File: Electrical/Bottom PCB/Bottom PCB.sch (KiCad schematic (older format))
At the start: 38 parts, among them J101 Steper1, J102 Steper2, SW101 FL, SW102 FR, U101 QRE1113, U102 ULN2003A, U103 MCP23017_SO, U104 QRE1113, U105 QRE1113, U106 QRE1113

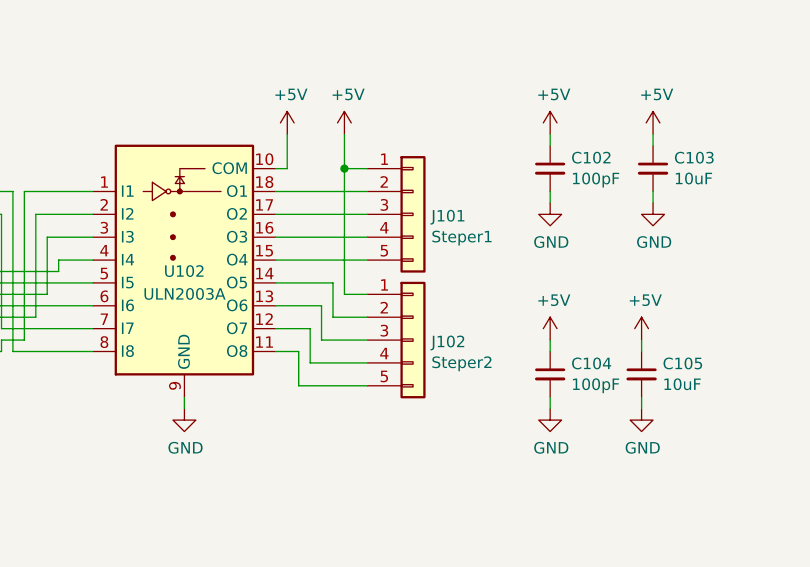
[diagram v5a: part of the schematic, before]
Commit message: changed from 1206 to 0805
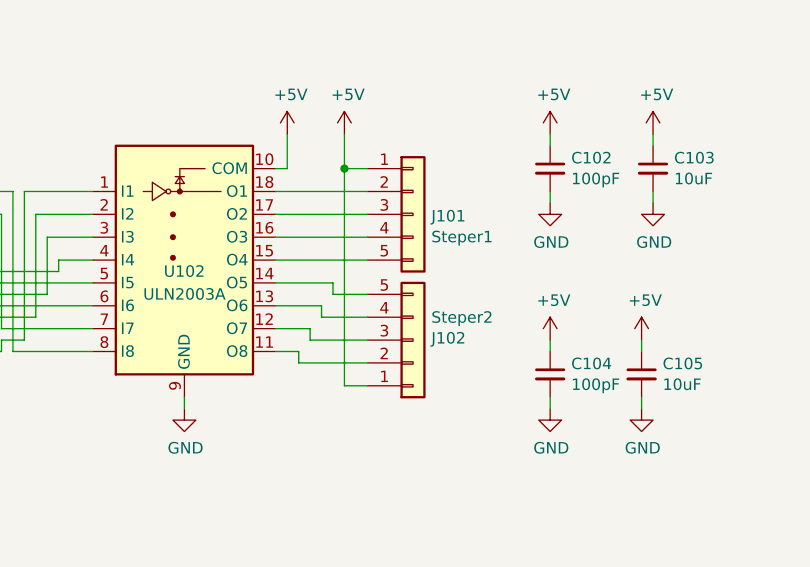
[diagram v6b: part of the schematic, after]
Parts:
- C101, C102, C103, C104, C105, C106, C107, C108: footprint Capacitor_SMD:C_1206_3216Metric_Pad1.42x1.75mm_HandSolder -> Capacitor_SMD:C_0805_2012Metric_Pad1.15x1.40mm_HandSolder
- R101, R102, R103, R104, R105, R106, R107, R108, R109, R110, R111, R112, R113, R114, R115: footprint Resistor_SMD:R_1206_3216Metric_Pad1.42x1.75mm_HandSolder -> Resistor_SMD:R_0805_2012Metric_Pad1.15x1.40mm_HandSolder
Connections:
- net at U102.11 (O8): now also J102.2 (Pin_2); no longer J102.5 (Pin_5)
- net at U102.12 (O7): now also J102.3 (Pin_3); no longer J102.4 (Pin_4)
- net at U102.13 (O6): now also J102.4 (Pin_4); no longer J102.3 (Pin_3)
- net at U102.14 (O5): now also J102.5 (Pin_5); no longer J102.2 (Pin_2)
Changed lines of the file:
@@
 F 0 "R104" H 1041 1904 50  0000 R CNN
 F 1 "10k" H 1041 1995 50  0000 R CNN
-F 2 "Resistor_SMD:R_1206_3216Metric_Pad1.42x1.75mm_HandSolder" H 1100 1950 50  0001 C CNN
+F 2 "Resistor_SMD:R_0805_2012Metric_Pad1.15x1.40mm_HandSolder" H 1100 1950 50  0001 C CNN
 F 3 "~" H 1100 1950 50  0001 C CNN
 	1    1100 1950
@@
 F 0 "R101" H 1041 1004 50  0000 R CNN
 F 1 "10k" H 1041 1095 50  0000 R CNN
-F 2 "Resistor_SMD:R_1206_3216Metric_Pad1.42x1.75mm_HandSolder" H 1100 1050 50  0001 C CNN
+F 2 "Resistor_SMD:R_0805_2012Metric_Pad1.15x1.40mm_HandSolder" H 1100 1050 50  0001 C CNN
 F 3 "~" H 1100 1050 50  0001 C CNN
 	1    1100 1050
@@
 F 0 "R106" H 1341 2704 50  0000 R CNN
 F 1 "10k" H 1341 2795 50  0000 R CNN
-F 2 "Resistor_SMD:R_1206_3216Metric_Pad1.42x1.75mm_HandSolder" H 1400 2750 50  0001 C CNN
+F 2 "Resistor_SMD:R_0805_2012Metric_Pad1.15x1.40mm_HandSolder" H 1400 2750 50  0001 C CNN
 F 3 "~" H 1400 2750 50  0001 C CNN
 	1    1400 2750
@@
 F 0 "R105" H 608 2704 50  0000 L CNN
 F 1 "100" H 608 2795 50  0000 L CNN
-F 2 "Resistor_SMD:R_1206_3216Metric_Pad1.42x1.75mm_HandSolder" H 550 2750 50  0001 C CNN
+F 2 "Resistor_SMD:R_0805_2012Metric_Pad1.15x1.40mm_HandSolder" H 550 2750 50  0001 C CNN
 F 3 "~" H 550 2750 50  0001 C CNN
 	1    550  2750
@@
 F 0 "C101" H 1492 3146 50  0000 L CNN
 F 1 "100pF" H 1492 3055 50  0000 L CNN
-F 2 "Capacitor_SMD:C_1206_3216Metric_Pad1.42x1.75mm_HandSolder" H 1400 3100 50  0001 C CNN
+F 2 "Capacitor_SMD:C_0805_2012Metric_Pad1.15x1.40mm_HandSolder" H 1400 3100 50  0001 C CNN
 F 3 "~" H 1400 3100 50  0001 C CNN
 	1    1400 3100
@@
 F 0 "R108" H 1341 4004 50  0000 R CNN
 F 1 "10k" H 1341 4095 50  0000 R CNN
-F 2 "Resistor_SMD:R_1206_3216Metric_Pad1.42x1.75mm_HandSolder" H 1400 4050 50  0001 C CNN
+F 2 "Resistor_SMD:R_0805_2012Metric_Pad1.15x1.40mm_HandSolder" H 1400 4050 50  0001 C CNN
 F 3 "~" H 1400 4050 50  0001 C CNN
 	1    1400 4050
@@
 F 0 "R107" H 608 4004 50  0000 L CNN
 F 1 "100" H 608 4095 50  0000 L CNN
-F 2 "Resistor_SMD:R_1206_3216Metric_Pad1.42x1.75mm_HandSolder" H 550 4050 50  0001 C CNN
+F 2 "Resistor_SMD:R_0805_2012Metric_Pad1.15x1.40mm_HandSolder" H 550 4050 50  0001 C CNN
 F 3 "~" H 550 4050 50  0001 C CNN
 	1    550  4050
@@
 F 0 "C106" H 1492 4446 50  0000 L CNN
 F 1 "100pF" H 1492 4355 50  0000 L CNN
-F 2 "Capacitor_SMD:C_1206_3216Metric_Pad1.42x1.75mm_HandSolder" H 1400 4400 50  0001 C CNN
+F 2 "Capacitor_SMD:C_0805_2012Metric_Pad1.15x1.40mm_HandSolder" H 1400 4400 50  0001 C CNN
 F 3 "~" H 1400 4400 50  0001 C CNN
 	1    1400 4400
@@
 F 0 "R113" H 1341 5254 50  0000 R CNN
 F 1 "10k" H 1341 5345 50  0000 R CNN
-F 2 "Resistor_SMD:R_1206_3216Metric_Pad1.42x1.75mm_HandSolder" H 1400 5300 50  0001 C CNN
+F 2 "Resistor_SMD:R_0805_2012Metric_Pad1.15x1.40mm_HandSolder" H 1400 5300 50  0001 C CNN
 F 3 "~" H 1400 5300 50  0001 C CNN
 	1    1400 5300
@@
 F 0 "R112" H 608 5254 50  0000 L CNN
 F 1 "100" H 608 5345 50  0000 L CNN
-F 2 "Resistor_SMD:R_1206_3216Metric_Pad1.42x1.75mm_HandSolder" H 550 5300 50  0001 C CNN
+F 2 "Resistor_SMD:R_0805_2012Metric_Pad1.15x1.40mm_HandSolder" H 550 5300 50  0001 C CNN
 F 3 "~" H 550 5300 50  0001 C CNN
 	1    550  5300
@@
 F 0 "C107" H 1492 5696 50  0000 L CNN
 F 1 "100pF" H 1492 5605 50  0000 L CNN
-F 2 "Capacitor_SMD:C_1206_3216Metric_Pad1.42x1.75mm_HandSolder" H 1400 5650 50  0001 C CNN
+F 2 "Capacitor_SMD:C_0805_2012Metric_Pad1.15x1.40mm_HandSolder" H 1400 5650 50  0001 C CNN
 F 3 "~" H 1400 5650 50  0001 C CNN
 	1    1400 5650
@@
 F 0 "C102" H 8542 3396 50  0000 L CNN
 F 1 "100pF" H 8542 3305 50  0000 L CNN
-F 2 "Capacitor_SMD:C_1206_3216Metric_Pad1.42x1.75mm_HandSolder" H 8450 3350 50  0001 C CNN
+F 2 "Capacitor_SMD:C_0805_2012Metric_Pad1.15x1.40mm_HandSolder" H 8450 3350 50  0001 C CNN
 F 3 "~" H 8450 3350 50  0001 C CNN
 	1    8450 3350
@@
 F 0 "C104" H 8542 4296 50  0000 L CNN
 F 1 "100pF" H 8542 4205 50  0000 L CNN
-F 2 "Capacitor_SMD:C_1206_3216Metric_Pad1.42x1.75mm_HandSolder" H 8450 4250 50  0001 C CNN
+F 2 "Capacitor_SMD:C_0805_2012Metric_Pad1.15x1.40mm_HandSolder" H 8450 4250 50  0001 C CNN
 F 3 "~" H 8450 4250 50  0001 C CNN
 	1    8450 4250
@@
 F 0 "C103" H 8992 3396 50  0000 L CNN
 F 1 "10uF" H 8992 3305 50  0000 L CNN
-F 2 "Capacitor_SMD:C_1206_3216Metric_Pad1.42x1.75mm_HandSolder" H 8900 3350 50  0001 C CNN
+F 2 "Capacitor_SMD:C_0805_2012Metric_Pad1.15x1.40mm_HandSolder" H 8900 3350 50  0001 C CNN
 F 3 "~" H 8900 3350 50  0001 C CNN
 	1    8900 3350
@@
 F 0 "C105" H 8942 4296 50  0000 L CNN
 F 1 "10uF" H 8942 4205 50  0000 L CNN
-F 2 "Capacitor_SMD:C_1206_3216Metric_Pad1.42x1.75mm_HandSolder" H 8850 4250 50  0001 C CNN
+F 2 "Capacitor_SMD:C_0805_2012Metric_Pad1.15x1.40mm_HandSolder" H 8850 4250 50  0001 C CNN
 F 3 "~" H 8850 4250 50  0001 C CNN
 	1    8850 4250
@@
 F 0 "C108" H 1492 7046 50  0000 L CNN
 F 1 "100pF" H 1492 6955 50  0000 L CNN
-F 2 "Capacitor_SMD:C_1206_3216Metric_Pad1.42x1.75mm_HandSolder" H 1400 7000 50  0001 C CNN
+F 2 "Capacitor_SMD:C_0805_2012Metric_Pad1.15x1.40mm_HandSolder" H 1400 7000 50  0001 C CNN
 F 3 "~" H 1400 7000 50  0001 C CNN
 	1    1400 7000
@@
 F 0 "R114" H 608 6604 50  0000 L CNN
 F 1 "100" H 608 6695 50  0000 L CNN
-F 2 "Resistor_SMD:R_1206_3216Metric_Pad1.42x1.75mm_HandSolder" H 550 6650 50  0001 C CNN
+F 2 "Resistor_SMD:R_0805_2012Metric_Pad1.15x1.40mm_HandSolder" H 550 6650 50  0001 C CNN
 F 3 "~" H 550 6650 50  0001 C CNN
 	1    550  6650
@@
 F 0 "R115" H 1341 6604 50  0000 R CNN
 F 1 "10k" H 1341 6695 50  0000 R CNN
-F 2 "Resistor_SMD:R_1206_3216Metric_Pad1.42x1.75mm_HandSolder" H 1400 6650 50  0001 C CNN
+F 2 "Resistor_SMD:R_0805_2012Metric_Pad1.15x1.40mm_HandSolder" H 1400 6650 50  0001 C CNN
 F 3 "~" H 1400 6650 50  0001 C CNN
 	1    1400 6650
@@
 F 0 "R109" H 3341 4654 50  0000 R CNN
 F 1 "47k" H 3341 4745 50  0000 R CNN
-F 2 "Resistor_SMD:R_1206_3216Metric_Pad1.42x1.75mm_HandSolder" H 3400 4700 50  0001 C CNN
+F 2 "Resistor_SMD:R_0805_2012Metric_Pad1.15x1.40mm_HandSolder" H 3400 4700 50  0001 C CNN
 F 3 "~" H 3400 4700 50  0001 C CNN
 	1    3400 4700
@@
 F 0 "R110" H 3691 4654 50  0000 R CNN
 F 1 "47k" H 3691 4745 50  0000 R CNN
-F 2 "Resistor_SMD:R_1206_3216Metric_Pad1.42x1.75mm_HandSolder" H 3750 4700 50  0001 C CNN
+F 2 "Resistor_SMD:R_0805_2012Metric_Pad1.15x1.40mm_HandSolder" H 3750 4700 50  0001 C CNN
 F 3 "~" H 3750 4700 50  0001 C CNN
 	1    3750 4700
@@
 F 0 "R111" H 4041 4654 50  0000 R CNN
 F 1 "47k" H 4041 4745 50  0000 R CNN
-F 2 "Resistor_SMD:R_1206_3216Metric_Pad1.42x1.75mm_HandSolder" H 4100 4700 50  0001 C CNN
+F 2 "Resistor_SMD:R_0805_2012Metric_Pad1.15x1.40mm_HandSolder" H 4100 4700 50  0001 C CNN
 F 3 "~" H 4100 4700 50  0001 C CNN
 	1    4100 4700
@@
 $EndComp
 Wire Wire Line
-	7350 4300 7650 4300
+	7350 4200 7650 4200
 Wire Wire Line
 	7350 4150 7250 4150
 Wire Wire Line
-	7350 4300 7350 4150
-Wire Wire Line
-	7400 4200 7650 4200
-Wire Wire Line
-	7400 4050 7400 4200
+	7350 4200 7350 4150
+Wire Wire Line
+	7400 4100 7650 4100
+Wire Wire Line
+	7400 4050 7400 4100
 Wire Wire Line
 	7250 4050 7400 4050
 Wire Wire Line
-	7450 3950 7450 4100
+	7450 3950 7450 4000
 Wire Wire Line
 	7250 3950 7450 3950
 Wire Wire Line
-	7500 3850 7500 4000
+	7500 3850 7500 3900
 Wire Wire Line
 	7250 3850 7500 3850
@@
 	7250 3450 7650 3450
 Wire Wire Line
-	7550 3350 7550 3900
+	7550 3350 7550 4300
 Connection ~ 7550 3350
 Wire Wire Line
 	7650 3350 7550 3350
-Wire Wire Line
-	7550 3900 7650 3900
 Wire Wire Line
 	7550 3200 7550 3350
@@
 $EndComp
 Wire Wire Line
-	7650 4100 7450 4100
-Wire Wire Line
-	7650 4000 7500 4000
+	7650 4000 7450 4000
+Wire Wire Line
+	7650 3900 7500 3900
 $Comp
 L Connector_Generic:Conn_01x05 J102
@@
 F 3 "~" H 7850 4100 50  0001 C CNN
 	1    7850 4100
-	1    0    0    -1
+	1    0    0    1
 $EndComp
 $Comp
@@
 F 0 "R102" V 7946 1200 50  0000 C CNN
 F 1 "2k7" V 7855 1200 50  0000 C CNN
-F 2 "Resistor_SMD:R_1206_3216Metric_Pad1.42x1.75mm_HandSolder" H 8050 1200 50  0001 C CNN
+F 2 "Resistor_SMD:R_0805_2012Metric_Pad1.15x1.40mm_HandSolder" H 8050 1200 50  0001 C CNN
 F 3 "~" H 8050 1200 50  0001 C CNN
 	1    8050 1200
@@
 F 0 "R103" H 7841 1354 50  0000 R CNN
 F 1 "4k7" H 7841 1445 50  0000 R CNN
-F 2 "Resistor_SMD:R_1206_3216Metric_Pad1.42x1.75mm_HandSolder" H 7900 1400 50  0001 C CNN
+F 2 "Resistor_SMD:R_0805_2012Metric_Pad1.15x1.40mm_HandSolder" H 7900 1400 50  0001 C CNN
 F 3 "~" H 7900 1400 50  0001 C CNN
 	1    7900 1400
@@
 	7900 1550 8200 1550
 Connection ~ 8200 1550
+Wire Wire Line
+	7550 4300 7650 4300
 $EndSCHEMATC

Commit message: hello
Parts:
- removed C101, C102, C104, C106, C107, C108: 100pF, Capacitor_SMD:C_0805_2012Metric_Pad1.15x1.40mm_HandSolder, symbol Device:C_Small
- removed C103, C105: 10uF, Capacitor_SMD:C_0805_2012Metric_Pad1.15x1.40mm_HandSolder, symbol Device:C_Small
- removed HC-SR101: HC-SR04, Connector_PinHeader_2.54mm:PinHeader_1x04_P2.54mm_Vertical, symbol Connector_Generic:Conn_01x04
- removed J101: Steper1, Connector_JST:JST_XH_B5B-XH-A_1x05_P2.50mm_Vertical, symbol Connector_Generic:Conn_01x05
- removed J102: Steper2, Connector_JST:JST_XH_B5B-XH-A_1x05_P2.50mm_Vertical, symbol Connector_Generic:Conn_01x05
- removed JP101: A2, Jumper:SolderJumper-2_P1.3mm_Open_Pad1.0x1.5mm, symbol Device:Jumper_NO_Small
- removed JP102: A1, Jumper:SolderJumper-2_P1.3mm_Open_Pad1.0x1.5mm, symbol Device:Jumper_NO_Small
- removed JP103: A0, Jumper:SolderJumper-2_P1.3mm_Open_Pad1.0x1.5mm, symbol Device:Jumper_NO_Small
- removed R101, R104, R106, R108, R113, R115: 10k, Resistor_SMD:R_0805_2012Metric_Pad1.15x1.40mm_HandSolder, symbol Device:R_Small
- removed R102: 2k7, Resistor_SMD:R_0805_2012Metric_Pad1.15x1.40mm_HandSolder, symbol Device:R_Small
- removed R103: 4k7, Resistor_SMD:R_0805_2012Metric_Pad1.15x1.40mm_HandSolder, symbol Device:R_Small
- removed R105, R107, R112, R114: 100, Resistor_SMD:R_0805_2012Metric_Pad1.15x1.40mm_HandSolder, symbol Device:R_Small
- removed R109, R110, R111: 47k, Resistor_SMD:R_0805_2012Metric_Pad1.15x1.40mm_HandSolder, symbol Device:R_Small
- removed SW101: FL, DF-M Series Micro Switches:TypeD, symbol DF-M_Series_Micro_Switches:DF-M_Series_Micro_Switch
- removed SW102: FR, DF-M Series Micro Switches:TypeC, symbol DF-M_Series_Micro_Switches:DF-M_Series_Micro_Switch
- removed U101, U104, U105, U106: QRE1113, OptoDevice:OnSemi_CASE100CY, symbol Sensor_Proximity:QRE1113
- removed U102: ULN2003A, Package_SO:SOIC-18W_7.5x11.6mm_P1.27mm, symbol Transistor_Array:ULN2803A
- removed U103: MCP23017_SO, Package_SO:SOIC-28W_7.5x17.9mm_P1.27mm, symbol Interface_Expansion:MCP23017_SO
